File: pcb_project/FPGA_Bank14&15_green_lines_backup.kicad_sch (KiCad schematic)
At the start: 39 parts, among them IC3 IS61WV204816BLL-10TLI, IC4 IS61WV204816BLL-10TLI, U1 XC7A100T-FTG256, U9 MT25QL128ABA1ESE-0SIT

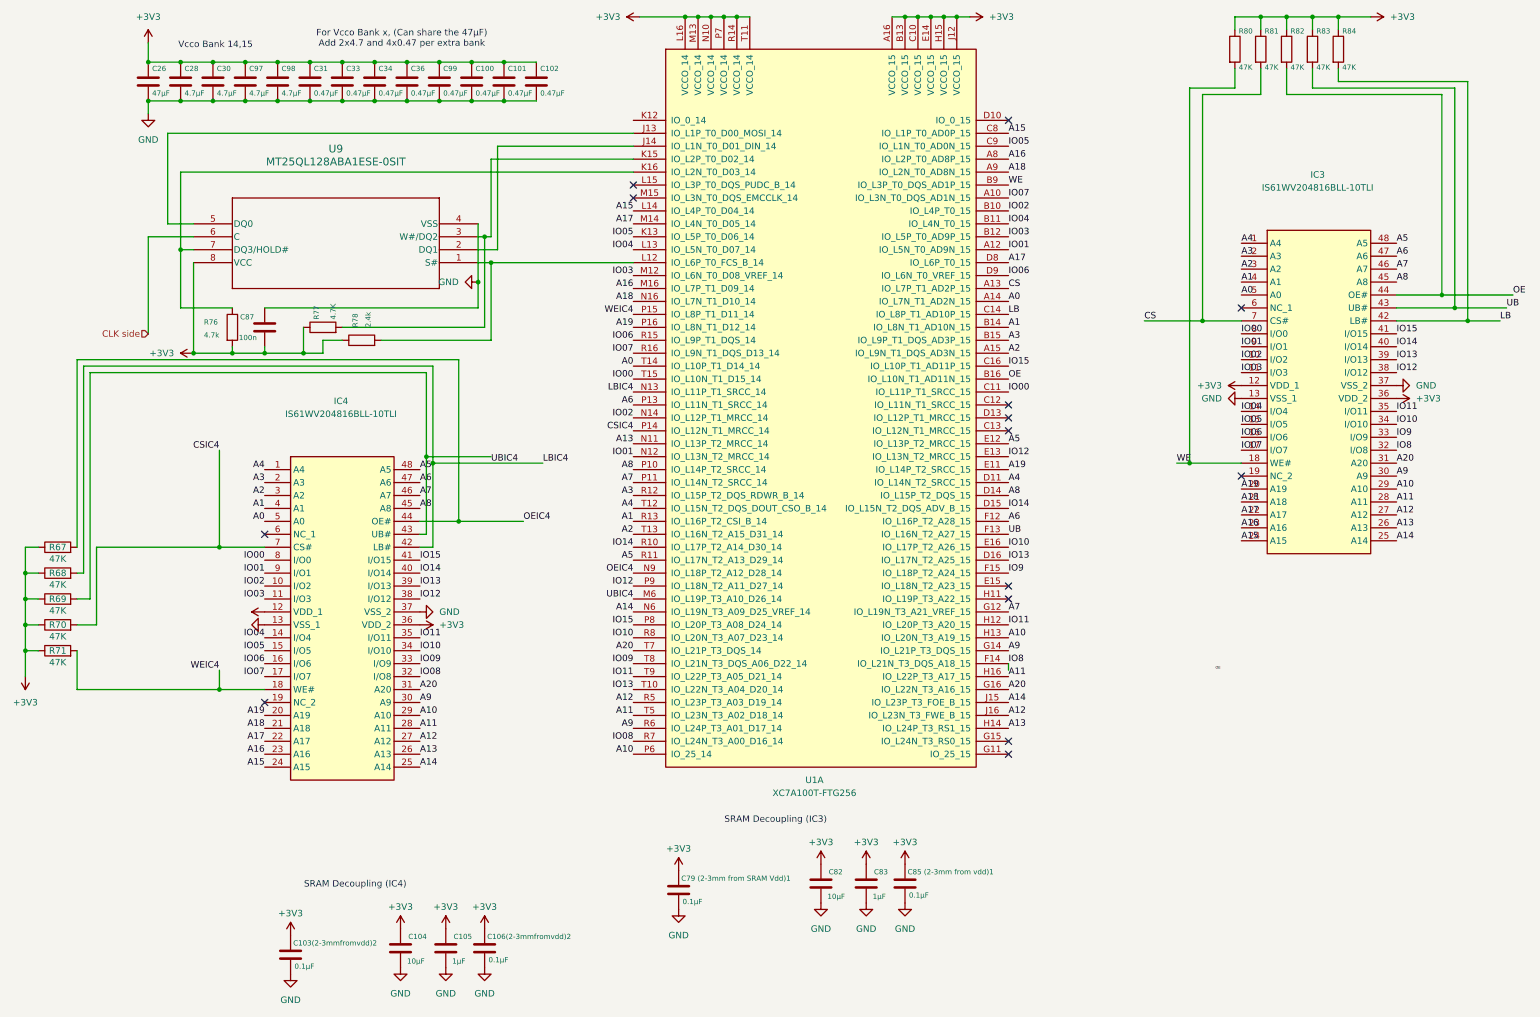
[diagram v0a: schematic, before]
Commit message: Fix IC4 missing FPGA pinouts with new labels
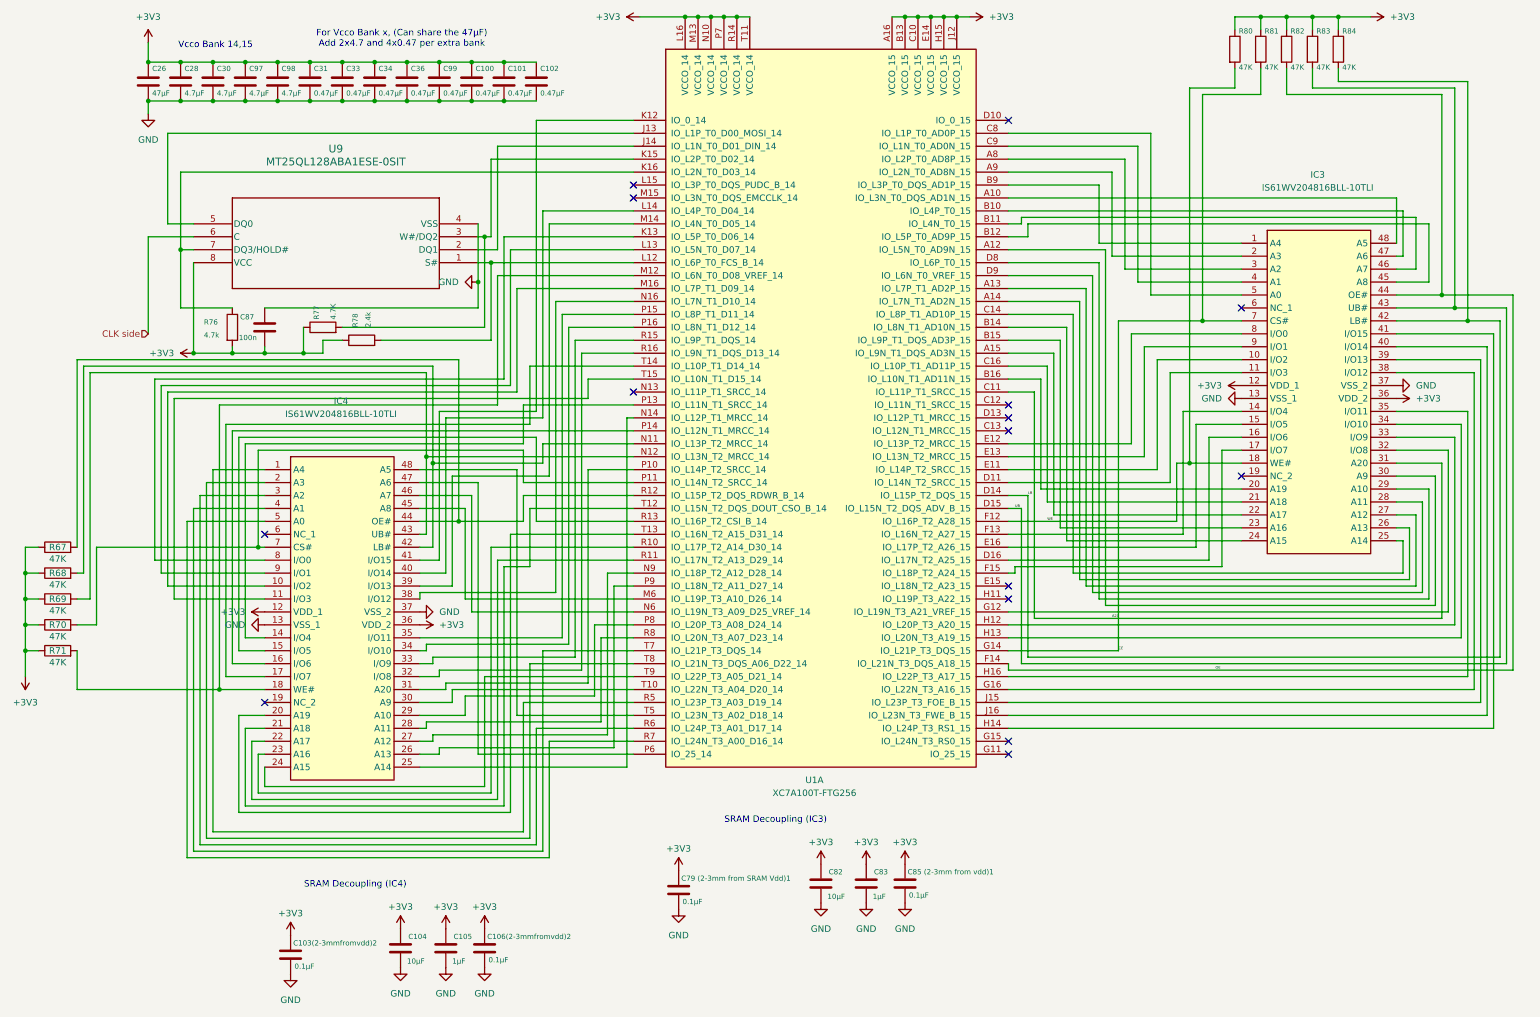
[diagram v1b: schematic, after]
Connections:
- net A20: now also U1.C11 (IO_L11P_T1_SRCC_15); no longer IC4.31 (A20), U1.G16 (IO_L22N_T3_A16_15), U1.T7 (IO_L21P_T3_DQS_14)
- net LB: now also U1.D14 (IO_L15P_T2_DQS_15); no longer U1.C14 (IO_L8P_T1_AD10P_15)
- net OE: now also U1.F14 (IO_L21N_T3_DQS_A18_15); no longer U1.B16 (IO_L10N_T1_AD11N_15)
- net UB: now also U1.D15 (IO_L15N_T2_DQS_ADV_B_15); no longer U1.F13 (IO_L16N_T2_A27_15)
- net WE: now also U1.F12 (IO_L16P_T2_A28_15); no longer U1.B9 (IO_L3P_T0_DQS_AD1P_15)
- net at IC4.43 (UB#), R69.2: now also U1.N12 (IO_L13N_T2_MRCC_14)
- net at U1.K12 (IO_0_14): now also IC4.41 (I/O15)
- removed net A0: IC3.5 (A0), IC4.5 (A0), U1.A14 (IO_L7N_T1_AD2N_15), U1.T14 (IO_L10P_T1_D14_14)
- removed net A1: IC3.4 (A1), IC4.4 (A1), U1.B14 (IO_L8N_T1_AD10N_15), U1.R13 (IO_L16P_T2_CSI_B_14)
- removed net A10: IC3.29 (A10), IC4.29 (A10), U1.H13 (IO_L20N_T3_A19_15), U1.P6 (IO_25_14)
- removed net A11: IC3.28 (A11), IC4.28 (A11), U1.H16 (IO_L22P_T3_A17_15), U1.T5 (IO_L23N_T3_A02_D18_14)
- removed net A12: IC3.27 (A12), IC4.27 (A12), U1.J16 (IO_L23N_T3_FWE_B_15), U1.R5 (IO_L23P_T3_A03_D19_14)
- removed net A13: IC3.26 (A13), IC4.26 (A13), U1.H14 (IO_L24P_T3_RS1_15), U1.N11 (IO_L13P_T2_MRCC_14)
- removed net A14: IC3.25 (A14), IC4.25 (A14), U1.J15 (IO_L23P_T3_FOE_B_15), U1.N6 (IO_L19N_T3_A09_D25_VREF_14)
- removed net A15: IC3.24 (A15), IC4.24 (A15), U1.C8 (IO_L1P_T0_AD0P_15), U1.L14 (IO_L4P_T0_D04_14)
- removed net A16: IC3.23 (A16), IC4.23 (A16), U1.A8 (IO_L2P_T0_AD8P_15), U1.M16 (IO_L7P_T1_D09_14)
- removed net A17: IC3.22 (A17), IC4.22 (A17), U1.D8 (IO_L6P_T0_15), U1.M14 (IO_L4N_T0_D05_14)
- removed net A18: IC3.21 (A18), IC4.21 (A18), U1.A9 (IO_L2N_T0_AD8N_15), U1.N16 (IO_L7N_T1_D10_14)
- removed net A19: IC3.20 (A19), IC4.20 (A19), U1.E11 (IO_L14P_T2_SRCC_15), U1.P16 (IO_L8N_T1_D12_14)
- removed net A2: IC3.3 (A2), IC4.3 (A2), U1.A15 (IO_L9N_T1_DQS_AD3N_15), U1.T13 (IO_L16N_T2_A15_D31_14)
- removed net A3: IC3.2 (A3), IC4.2 (A3), U1.B15 (IO_L9P_T1_DQS_AD3P_15), U1.R12 (IO_L15P_T2_DQS_RDWR_B_14)
- removed net A4: IC3.1 (A4), IC4.1 (A4), U1.D11 (IO_L14N_T2_SRCC_15), U1.T12 (IO_L15N_T2_DQS_DOUT_CSO_B_14)
- removed net A5: IC3.48 (A5), IC4.48 (A5), U1.E12 (IO_L13P_T2_MRCC_15), U1.R11 (IO_L17N_T2_A13_D29_14)
- removed net A6: IC3.47 (A6), IC4.47 (A6), U1.F12 (IO_L16P_T2_A28_15), U1.P13 (IO_L11N_T1_SRCC_14)
- removed net A7: IC3.46 (A7), IC4.46 (A7), U1.G12 (IO_L19N_T3_A21_VREF_15), U1.P11 (IO_L14N_T2_SRCC_14)
- removed net A8: IC3.45 (A8), IC4.45 (A8), U1.D14 (IO_L15P_T2_DQS_15), U1.P10 (IO_L14P_T2_SRCC_14)
- removed net A9: IC3.30 (A9), IC4.30 (A9), U1.G14 (IO_L21P_T3_DQS_15), U1.R6 (IO_L24P_T3_A01_D17_14)
- net CS renamed CE
- net CE: now also U1.G14 (IO_L21P_T3_DQS_15); no longer U1.A13 (IO_L7P_T1_AD2P_15)
- net CSIC4: no longer names the net of IC4.7 (CS#), R70.2
- net CSIC4: now also U1.P11 (IO_L14N_T2_SRCC_14); no longer U1.P14 (IO_L12N_T1_MRCC_14)
- removed net IO00: IC3.8 (I/O0), IC4.8 (I/O0), U1.C11 (IO_L11P_T1_SRCC_15), U1.T15 (IO_L10N_T1_D15_14)
- removed net IO01: IC3.9 (I/O1), IC4.9 (I/O1), U1.A12 (IO_L5N_T0_AD9N_15), U1.N12 (IO_L13N_T2_MRCC_14)
- removed net IO02: IC3.10 (I/O2), IC4.10 (I/O2), U1.B10 (IO_L4P_T0_15), U1.N14 (IO_L12P_T1_MRCC_14)
- removed net IO03: IC3.11 (I/O3), IC4.11 (I/O3), U1.B12 (IO_L5P_T0_AD9P_15), U1.M12 (IO_L6N_T0_D08_VREF_14)
- removed net IO04: IC3.14 (I/O4), IC4.14 (I/O4), U1.B11 (IO_L4N_T0_15), U1.L13 (IO_L5N_T0_D07_14)
- removed net IO05: IC3.15 (I/O5), IC4.15 (I/O5), U1.C9 (IO_L1N_T0_AD0N_15), U1.K13 (IO_L5P_T0_D06_14)
- removed net IO06: IC3.16 (I/O6), IC4.16 (I/O6), U1.D9 (IO_L6N_T0_VREF_15), U1.R15 (IO_L9P_T1_DQS_14)
- removed net IO07: IC3.17 (I/O7), IC4.17 (I/O7), U1.A10 (IO_L3N_T0_DQS_AD1N_15), U1.R16 (IO_L9N_T1_DQS_D13_14)
- net IO08: no longer names the net of IC4.32 (I/O8)
- net IO08: now also U1.R16 (IO_L9N_T1_DQS_D13_14); no longer U1.R7 (IO_L24N_T3_A00_D16_14)
- net IO09: no longer names the net of IC4.33 (I/O9)
- net IO09: now also U1.R15 (IO_L9P_T1_DQS_14); no longer U1.T8 (IO_L21N_T3_DQS_A06_D22_14)
- removed net IO10: IC3.34 (I/O10), IC4.34 (I/O10), U1.E16 (IO_L17P_T2_A26_15), U1.R8 (IO_L20N_T3_A07_D23_14)
- removed net IO11: IC3.35 (I/O11), IC4.35 (I/O11), U1.H12 (IO_L20P_T3_A20_15), U1.T9 (IO_L22P_T3_A05_D21_14)
- removed net IO12: IC3.38 (I/O12), IC4.38 (I/O12), U1.E13 (IO_L13N_T2_MRCC_15), U1.P9 (IO_L18N_T2_A11_D27_14)
- removed net IO13: IC3.39 (I/O13), IC4.39 (I/O13), U1.D16 (IO_L17N_T2_A25_15), U1.T10 (IO_L22N_T3_A04_D20_14)
- removed net IO14: IC3.40 (I/O14), IC4.40 (I/O14), U1.D15 (IO_L15N_T2_DQS_ADV_B_15), U1.R10 (IO_L17P_T2_A14_D30_14)
- removed net IO15: IC3.41 (I/O15), IC4.41 (I/O15), U1.C16 (IO_L10P_T1_AD11P_15), U1.P8 (IO_L20P_T3_A08_D24_14)
- net IO8: no longer names the net of IC3.32 (I/O8)
- net IO8: now also U1.G12 (IO_L19N_T3_A21_VREF_15); no longer U1.F14 (IO_L21N_T3_DQS_A18_15)
- net IO9: no longer names the net of U1.F15 (IO_L18P_T2_A24_15)
- net IO9: now also IC3.17 (I/O7); no longer IC3.33 (I/O9)
- net LBIC4: no longer names the net of IC4.42 (LB#), R68.2
- net LBIC4: now also U1.N11 (IO_L13P_T2_MRCC_14); no longer U1.M6 (IO_L19P_T3_A10_D26_14), U1.N13 (IO_L11P_T1_SRCC_14)
- net OEIC4: no longer names the net of IC4.44 (OE#), R67.2
- net OEIC4: now also U1.R12 (IO_L15P_T2_DQS_RDWR_B_14); no longer U1.N9 (IO_L18P_T2_A12_D28_14)
- net WEIC4: no longer names the net of IC4.18 (WE#), R71.2
- net WEIC4: now also U1.M12 (IO_L6N_T0_D08_VREF_14); no longer U1.P15 (IO_L8P_T1_D11_14)
- new net: IC3.1 (A4), U1.B9 (IO_L3P_T0_DQS_AD1P_15)
- new net: IC3.10 (I/O2), U1.E11 (IO_L14P_T2_SRCC_15)
- new net: IC3.11 (I/O3), U1.D11 (IO_L14N_T2_SRCC_15)
- new net: IC3.14 (I/O4), U1.F13 (IO_L16N_T2_A27_15)
- new net: IC3.15 (I/O5), U1.E16 (IO_L17P_T2_A26_15)
- new net: IC3.16 (I/O6), U1.D16 (IO_L17N_T2_A25_15)
- new net: IC3.2 (A3), U1.A9 (IO_L2N_T0_AD8N_15)
- new net: IC3.20 (A19), U1.B16 (IO_L10N_T1_AD11N_15)
- new net: IC3.21 (A18), U1.C16 (IO_L10P_T1_AD11P_15)
- new net: IC3.22 (A17), U1.A15 (IO_L9N_T1_DQS_AD3N_15)
- new net: IC3.23 (A16), U1.B15 (IO_L9P_T1_DQS_AD3P_15)
- new net: IC3.24 (A15), U1.B14 (IO_L8N_T1_AD10N_15)
- new net: IC3.25 (A14), U1.C14 (IO_L8P_T1_AD10P_15)
- new net: IC3.26 (A13), U1.A14 (IO_L7N_T1_AD2N_15)
- new net: IC3.27 (A12), U1.A13 (IO_L7P_T1_AD2P_15)
- new net: IC3.28 (A11), U1.D9 (IO_L6N_T0_VREF_15)
- new net: IC3.29 (A10), U1.D8 (IO_L6P_T0_15)
- new net: IC3.3 (A2), U1.A8 (IO_L2P_T0_AD8P_15)
- new net: IC3.30 (A9), U1.A12 (IO_L5N_T0_AD9N_15)
- new net: IC3.33 (I/O9), U1.H12 (IO_L20P_T3_A20_15)
- new net: IC3.34 (I/O10), U1.H13 (IO_L20N_T3_A19_15)
- new net: IC3.35 (I/O11), U1.H16 (IO_L22P_T3_A17_15)
- new net: IC3.38 (I/O12), U1.G16 (IO_L22N_T3_A16_15)
- new net: IC3.39 (I/O13), U1.J15 (IO_L23P_T3_FOE_B_15)
- new net: IC3.4 (A1), U1.C9 (IO_L1N_T0_AD0N_15)
- new net: IC3.40 (I/O14), U1.J16 (IO_L23N_T3_FWE_B_15)
- new net: IC3.41 (I/O15), U1.H14 (IO_L24P_T3_RS1_15)
- new net: IC3.45 (A8), U1.B12 (IO_L5P_T0_AD9P_15)
- new net: IC3.46 (A7), U1.B11 (IO_L4N_T0_15)
- new net: IC3.47 (A6), U1.B10 (IO_L4P_T0_15)
- new net: IC3.48 (A5), U1.A10 (IO_L3N_T0_DQS_AD1N_15)
- new net: IC3.5 (A0), U1.C8 (IO_L1P_T0_AD0P_15)
- new net: IC3.8 (I/O0), U1.E12 (IO_L13P_T2_MRCC_15)
- new net: IC3.9 (I/O1), U1.E13 (IO_L13N_T2_MRCC_15)
- new net: IC4.8 (I/O0), U1.K13 (IO_L5P_T0_D06_14)
- new net: IC4.9 (I/O1), U1.L13 (IO_L5N_T0_D07_14)
- new net: IC4.40 (I/O14), U1.L14 (IO_L4P_T0_D04_14)
- new net: IC4.39 (I/O13), U1.M14 (IO_L4N_T0_D05_14)
- new net: IC4.10 (I/O2), U1.M16 (IO_L7P_T1_D09_14)
- new net: IC4.45 (A8), U1.M6 (IO_L19P_T3_A10_D26_14)
- new net: IC4.25 (A14), U1.N14 (IO_L12P_T1_MRCC_14)
- new net: IC4.38 (I/O12), U1.N16 (IO_L7N_T1_D10_14)
- new net: IC4.46 (A7), U1.N6 (IO_L19N_T3_A09_D25_VREF_14)
- new net: IC4.27 (A12), U1.N9 (IO_L18P_T2_A12_D28_14)
- new net: IC4.31 (A20), U1.P10 (IO_L14P_T2_SRCC_14)
- new net: IC4.14 (I/O4), U1.P13 (IO_L11N_T1_SRCC_14)
- new net: IC4.16 (I/O6), U1.P14 (IO_L12N_T1_MRCC_14)
- new net: IC4.35 (I/O11), U1.P15 (IO_L8P_T1_D11_14)
- new net: IC4.34 (I/O10), U1.P16 (IO_L8N_T1_D12_14)
- new net: IC4.47 (A6), U1.P6 (IO_25_14)
- new net: IC4.29 (A10), U1.P8 (IO_L20P_T3_A08_D24_14)
- new net: IC4.26 (A13), U1.P9 (IO_L18N_T2_A11_D27_14)
- new net: IC4.23 (A16), U1.R10 (IO_L17P_T2_A14_D30_14)
- new net: IC4.22 (A17), U1.R11 (IO_L17N_T2_A13_D29_14)
- new net: IC4.15 (I/O5), U1.R13 (IO_L16P_T2_CSI_B_14)
- new net: IC4.1 (A4), U1.R5 (IO_L23P_T3_A03_D19_14)
- new net: IC4.3 (A2), U1.R6 (IO_L24P_T3_A01_D17_14)
- new net: IC4.5 (A0), U1.R7 (IO_L24N_T3_A00_D16_14)
- new net: IC4.28 (A11), U1.R8 (IO_L20N_T3_A07_D23_14)
- new net: IC4.30 (A9), U1.T10 (IO_L22N_T3_A04_D20_14)
- new net: IC4.21 (A18), U1.T12 (IO_L15N_T2_DQS_DOUT_CSO_B_14)
- new net: IC4.20 (A19), U1.T13 (IO_L16N_T2_A15_D31_14)
- new net: IC4.17 (I/O7), U1.T14 (IO_L10P_T1_D14_14)
- new net: IC4.11 (I/O3), U1.T15 (IO_L10N_T1_D15_14)
- new net: IC4.48 (A5), U1.T5 (IO_L23N_T3_A02_D18_14)
- new net: IC4.4 (A1), U1.T7 (IO_L21P_T3_DQS_14)
- new net: IC4.2 (A3), U1.T8 (IO_L21N_T3_DQS_A06_D22_14)
- new net: IC4.24 (A15), U1.T9 (IO_L22P_T3_A05_D21_14)
- no-connect marks 14 -> 15
